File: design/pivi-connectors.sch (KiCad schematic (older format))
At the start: 16 parts, among them P2 CONN_01X02, P3 Recom_Power_RAC10-05SC/277, P4 CONN_01X02, P5 CONN_02X20, P6 CONN_01X04, P7 CONN_01X02

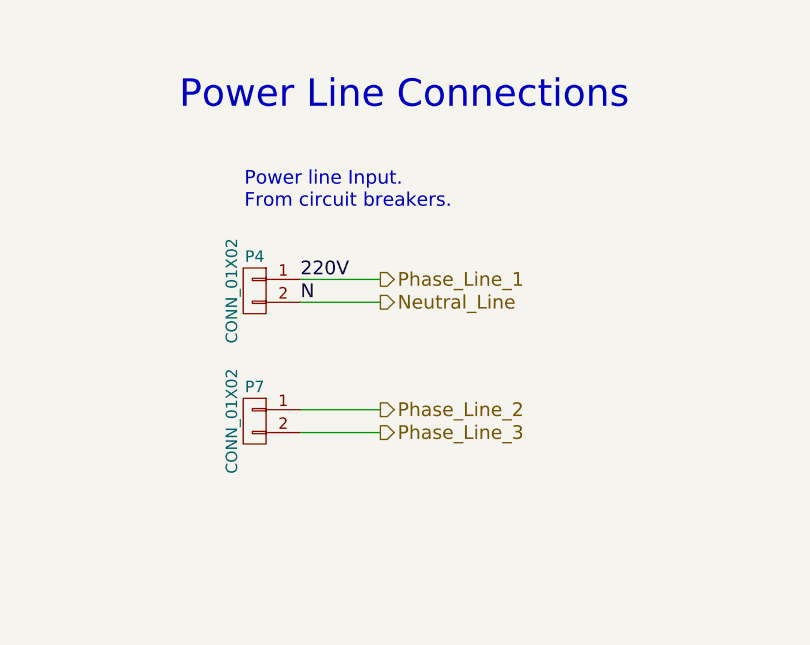
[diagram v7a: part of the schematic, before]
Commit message: Fix #11: Terminal block is not appropriated.
Changed 2 positions terminal block to a 4 positions terminal block.
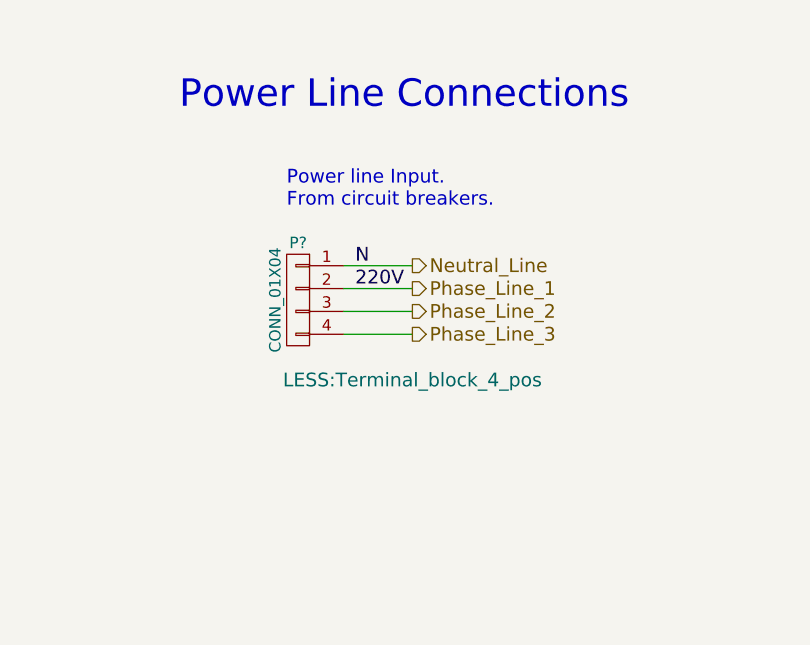
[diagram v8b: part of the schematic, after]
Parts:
- removed P4, P7: CONN_01X02, Connect:bornier2, symbol CONN_01X02
- added P?: CONN_01X04, LESS:Terminal_block_4_pos, symbol CONN_01X04
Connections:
- net Neutral_Line: now also P?.1 (P1)
- net Phase_Line_1: now also P?.2 (P2)
- net Phase_Line_2: now also P?.3 (P3)
- net Phase_Line_3: now also P?.4 (P4)
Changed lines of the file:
@@
 NoConn ~ 7015 1865
 NoConn ~ 7015 1765
-Text Notes 6015 4855 0    60   ~ 0
+Text Notes 6200 4850 0    60   ~ 0
 Power line Input.\nFrom circuit breakers.
 $Comp
@@
 Text Notes 1250 4445 0    120  ~ 0
 Board power Supply Connections
-Text HLabel 6610 5160 2    60   Output ~ 0
+Text HLabel 6750 5200 2    60   Output ~ 0
 Phase_Line_1
-Text HLabel 6610 5260 2    60   Output ~ 0
+Text HLabel 6750 5100 2    60   Output ~ 0
 Neutral_Line
-Text Label 6260 5160 0    60   ~ 0
+Text Label 6500 5200 0    60   ~ 0
 220V
-Text Label 6260 5260 0    60   ~ 0
+Text Label 6500 5100 0    60   ~ 0
 N
 Text Label 1300 5170 2    60   ~ 0
@@
 Place inductors close to the \npower supply.
 $Comp
-L CONN_01X02 P4
-U 1 1 54C3B67F
-P 6060 5210
-F 0 "P4" H 6060 5360 50  0000 C CNN
-F 1 "CONN_01X02" V 6160 5210 50  0000 C CNN
-F 2 "Connect:bornier2" H 6060 5210 60  0001 C CNN
-F 3 "" H 6060 5210 60  0000 C CNN
-	1    6060 5210
-	-1   0    0    -1
-$EndComp
-$Comp
 L Recom_Power_RAC10-05SC/277 P3
 U 1 1 54C3C5E9
@@
 Wire Wire Line
 	7590 1365 7515 1365
-Wire Wire Line
-	6260 5260 6610 5260
-Wire Wire Line
-	6260 5160 6610 5160
 Wire Wire Line
 	2625 5170 2625 5270
@@
 Wire Wire Line
 	9070 5205 9240 5205
-Text HLabel 6610 5730 2    60   Output ~ 0
+Text HLabel 6750 5300 2    60   Output ~ 0
 Phase_Line_2
-Text HLabel 6610 5830 2    60   Output ~ 0
+Text HLabel 6750 5400 2    60   Output ~ 0
 Phase_Line_3
 $Comp
-L CONN_01X02 P7
-U 1 1 55BC87D7
-P 6060 5780
-F 0 "P7" H 6060 5930 50  0000 C CNN
-F 1 "CONN_01X02" V 6160 5780 50  0000 C CNN
-F 2 "Connect:bornier2" H 6060 5780 60  0001 C CNN
-F 3 "" H 6060 5780 60  0000 C CNN
-	1    6060 5780
+L CONN_01X04 P?
+U 1 1 55F7C621
+P 6250 5250
+F 0 "P?" H 6250 5500 50  0000 C CNN
+F 1 "CONN_01X04" V 6350 5250 50  0000 C CNN
+F 2 "LESS:Terminal_block_4_pos" H 5750 4900 60  0000 C CNN
+F 3 "" H 6250 5250 60  0000 C CNN
+	1    6250 5250
 	-1   0    0    -1
 $EndComp
 Wire Wire Line
-	6260 5830 6610 5830
-Wire Wire Line
-	6260 5730 6610 5730
+	6450 5100 6750 5100
+Wire Wire Line
+	6450 5200 6750 5200
+Wire Wire Line
+	6450 5300 6750 5300
+Wire Wire Line
+	6450 5400 6750 5400
 $EndSCHEMATC
